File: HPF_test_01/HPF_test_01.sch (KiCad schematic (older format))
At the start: 7 parts, among them T1 GT07-110-013

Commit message: Reorganized and added footprints and symbols, .sch reflects changes
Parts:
- removed C2: 510nF, symbol pspice:C
- removed SL1002A600SP: GDT, symbol GT07:GDT
- removed SMCJ5.0A: TVS, symbol Device:D_TVS
- removed VP4032K122R300: MOV, symbol GT07:MOV
- added C2: ECQ-UBAF474K, ECQUBAF474K, symbol ECQ-UBAF474K:ECQ-UBAF474K
- added D1: SMCJ5.0A, DIONM7959X262N, symbol SMCJ5.0A:SMCJ5.0A
- added J1: BNC5-J-P-GN-RA-BH2D, BNC5-J-P-GN-RA-BH2D_kicad:BNC5JPGNRABH2D, symbol BNC5-J-P-GN-RA-BH2D:BNC5-J-P-GN-RA-BH2D
- added RV1: VP4032K122R300, CAPPM10080X500N, symbol VP4032K122R300:VP4032K122R300
- added U1: SL1002A600SP, SL1002A600SP, symbol SL1002A600SP:SL1002A600SP
- C1: footprint (none) -> Capacitor_SMD:C_0603_1608Metric_Pad1.05x0.95mm_HandSolder
- T1: footprint GT07110013 -> Kicad-GT07-models:GT07110013
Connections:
- net labels removed: out
- wire segments 22 -> 30
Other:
- moved on the sheet: C1
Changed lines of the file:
@@
 L pspice:C C1
 U 1 1 619514BE
-P 7500 4300
-F 0 "C1" H 7322 4254 50  0000 R CNN
-F 1 "220pF" H 7322 4345 50  0000 R CNN
-F 2 "" H 7500 4300 50  0001 C CNN
-F 3 "~" H 7500 4300 50  0001 C CNN
-F 4 "C" H 7500 4300 50  0001 C CNN "Spice_Primitive"
-F 5 "220p" H 7500 4300 50  0001 C CNN "Spice_Model"
-F 6 "Y" H 7500 4300 50  0001 C CNN "Spice_Netlist_Enabled"
-	1    7500 4300
+P 7450 4300
+F 0 "C1" H 7272 4254 50  0000 R CNN
+F 1 "220pF" H 7272 4345 50  0000 R CNN
+F 2 "Capacitor_SMD:C_0603_1608Metric_Pad1.05x0.95mm_HandSolder" H 7450 4300 50  0001 C CNN
+F 3 "~" H 7450 4300 50  0001 C CNN
+F 4 "C" H 7450 4300 50  0001 C CNN "Spice_Primitive"
+F 5 "220p" H 7450 4300 50  0001 C CNN "Spice_Model"
+F 6 "Y" H 7450 4300 50  0001 C CNN "Spice_Netlist_Enabled"
+	1    7450 4300
 	-1   0    0    1
-$EndComp
-Text GLabel 7600 3850 2    50   Input ~ 0
-out
-$Comp
-L pspice:0 #GND02
-U 1 1 61961008
-P 7500 4850
-F 0 "#GND02" H 7500 4750 50  0001 C CNN
-F 1 "0" H 7500 4900 50  0000 C CNN
-F 2 "" H 7500 4850 50  0001 C CNN
-F 3 "~" H 7500 4850 50  0001 C CNN
-	1    7500 4850
-	1    0    0    -1
 $EndComp
 $Comp
@@
 F 0 "T1" H 5650 4465 50  0000 C CNN
 F 1 "GT07-110-013" H 5650 4374 50  0000 C CNN
-F 2 "GT07110013" H 6200 4300 50  0001 L CNN
+F 2 "Kicad-GT07-models:GT07110013" H 6200 4300 50  0001 L CNN
 F 3 "https://componentsearchengine.com/Datasheets/1/GT07-110-013.pdf" H 6200 4200 50  0001 L CNN
 F 4 "Pulse Transformers" H 6200 4100 50  0001 L CNN "Description"
@@
 NoConn ~ 6350 4300
 NoConn ~ 4950 4300
-$Comp
-L Device:D_TVS SMCJ5.0A
-U 1 1 61BE143F
-P 6700 4300
-F 0 "SMCJ5.0A" V 6654 4380 50  0000 L CNN
-F 1 "TVS" V 6745 4380 50  0000 L CNN
-F 2 "" H 6700 4300 50  0001 C CNN
-F 3 "https://www.littelfuse.com/~/media/electronics/datasheets/tvs_diodes/littelfuse_tvs_diode_smcj_datasheet.pdf.pdf" H 6700 4300 50  0001 C CNN
-	1    6700 4300
-	0    1    1    0
-$EndComp
-$Comp
-L GT07:GDT SL1002A600SP
-U 1 1 61BE33A2
-P 4050 4000
-F 0 "SL1002A600SP" H 4278 4046 50  0000 L CNN
-F 1 "GDT" H 4278 3955 50  0000 L CNN
-F 2 "" H 4050 4000 50  0001 C CNN
-F 3 "https://www.mouser.com/datasheet/2/240/Littelfuse_GDT_SL1002A_Datasheet.pdf-1317360.pdf" H 4050 4000 50  0001 C CNN
-	1    4050 4000
-	1    0    0    -1
-$EndComp
-$Comp
-L pspice:C C2
-U 1 1 6194BCFB
-P 4550 5100
-F 0 "C2" V 4300 5100 50  0000 C CNN
-F 1 "510nF" V 4200 5100 50  0000 C CNN
-F 2 "" H 4550 5100 50  0001 C CNN
-F 3 "~" H 4550 5100 50  0001 C CNN
-F 4 "C" H 4550 5100 50  0001 C CNN "Spice_Primitive"
-F 5 "510n" H 4550 5100 50  0001 C CNN "Spice_Model"
-F 6 "Y" H 4550 5100 50  0001 C CNN "Spice_Netlist_Enabled"
-	1    4550 5100
-	0    -1   -1   0
-$EndComp
-Wire Wire Line
-	4050 3600 4950 3600
 Wire Wire Line
 	4950 3600 4950 4200
-$Comp
-L GT07:MOV VP4032K122R300
-U 1 1 61BE8782
-P 4050 4750
-F 0 "VP4032K122R300" H 4178 4796 50  0000 L CNN
-F 1 "MOV" H 4178 4705 50  0000 L CNN
-F 2 "" H 4100 4800 50  0001 C CNN
-F 3 "https://content.kemet.com/datasheets/KEM_V0005_VP.pdf" H 4100 4800 50  0001 C CNN
-	1    4050 4750
-	1    0    0    -1
-$EndComp
 Wire Wire Line
 	4950 5100 4800 5100
@@
 	4950 4400 4950 5100
 Wire Wire Line
-	4300 5100 4050 5100
-Wire Wire Line
-	4050 5100 3000 5100
-Wire Wire Line
 	3000 5100 3000 5250
-Connection ~ 4050 5100
 Wire Wire Line
 	3000 4550 3000 5100
@@
 Wire Wire Line
 	3000 3950 3000 3600
-Wire Wire Line
-	3000 3600 4050 3600
-Connection ~ 4050 3600
-Wire Wire Line
-	6350 4400 6350 4700
-Wire Wire Line
-	6350 4700 6700 4700
-Wire Wire Line
-	6350 4200 6350 3850
-Wire Wire Line
-	6350 3850 6700 3850
-Wire Wire Line
-	6700 4150 6700 3850
-Connection ~ 6700 3850
-Wire Wire Line
-	6700 4450 6700 4700
-Connection ~ 6700 4700
-Wire Wire Line
-	6700 3850 7500 3850
-Wire Wire Line
-	7500 3850 7500 4050
-Connection ~ 7500 3850
-Wire Wire Line
-	7500 3850 7600 3850
-Wire Wire Line
-	7500 4550 7500 4700
-Wire Wire Line
-	7500 4700 7500 4850
-Connection ~ 7500 4700
-Wire Wire Line
-	6700 4700 7500 4700
 Text Notes 6700 5150 0    50   ~ 0
 TVS: \n5V standoff\n6.4-7V breakdown \n9.2V max clamping
@@
 Text Notes 3500 5650 0    50   ~ 0
 MOV:\n300V rms rating\n385VDC\n470V Varistor V (typ)\n1.2kA surge I\n30J
+$Comp
+L VP4032K122R300:VP4032K122R300 RV1
+U 1 1 61CA4EFC
+P 4050 4250
+F 0 "RV1" V 4354 4378 50  0000 L CNN
+F 1 "VP4032K122R300" V 4445 4378 50  0000 L CNN
+F 2 "CAPPM10080X500N" H 4600 4300 50  0001 L CNN
+F 3 "https://www.arrow.com/en/products/vp4032k122r300/kemet-corporation?region=nac" H 4600 4200 50  0001 L CNN
+F 4 "Varistors 385V 1200A 4032" H 4600 4100 50  0001 L CNN "Description"
+F 5 "5" H 4600 4000 50  0001 L CNN "Height"
+F 6 "80-VP4032K122R300" H 4600 3900 50  0001 L CNN "Mouser Part Number"
+F 7 "https://www.mouser.co.uk/ProductDetail/KEMET/VP4032K122R300?qs=jj7GbYRQuOYGBVagWkrU5w%3D%3D" H 4600 3800 50  0001 L CNN "Mouser Price/Stock"
+F 8 "Kemet" H 4600 3700 50  0001 L CNN "Manufacturer_Name"
+F 9 "VP4032K122R300" H 4600 3600 50  0001 L CNN "Manufacturer_Part_Number"
+	1    4050 4250
+	0    1    1    0
+$EndComp
+$Comp
+L SL1002A600SP:SL1002A600SP U1
+U 1 1 61CA5911
+P 4050 4050
+F 0 "U1" H 4342 3685 50  0000 C CNN
+F 1 "SL1002A600SP" H 4342 3776 50  0000 C CNN
+F 2 "SL1002A600SP" H 4700 4150 50  0001 L CNN
+F 3 "https://componentsearchengine.com/Datasheets/1/SL1002A600SP.pdf" H 4700 4050 50  0001 L CNN
+F 4 "Gas Discharge Tubes - GDTs / Gas Plasma Arrestors GP MINIBETA 2T A600V SMD SPECIAL" H 4700 3950 50  0001 L CNN "Description"
+F 5 "4.1" H 4700 3850 50  0001 L CNN "Height"
+F 6 "576-SL1002A600SP" H 4700 3750 50  0001 L CNN "Mouser Part Number"
+F 7 "https://www.mouser.co.uk/ProductDetail/Littelfuse/SL1002A600SP?qs=95aqoVzNh5Z3taNZSmSH3g%3D%3D" H 4700 3650 50  0001 L CNN "Mouser Price/Stock"
+F 8 "LITTELFUSE" H 4700 3550 50  0001 L CNN "Manufacturer_Name"
+F 9 "SL1002A600SP" H 4700 3450 50  0001 L CNN "Manufacturer_Part_Number"
+	1    4050 4050
+	-1   0    0    1
+$EndComp
+Wire Wire Line
+	3000 3600 4050 3600
+Wire Wire Line
+	3000 5100 4050 5100
+Wire Wire Line
+	4050 4250 4050 4050
+Wire Wire Line
+	4050 3950 4050 3600
+Connection ~ 4050 3600
+Wire Wire Line
+	4050 3600 4950 3600
+Wire Wire Line
+	4050 4950 4050 5100
+Connection ~ 4050 5100
+Wire Wire Line
+	4050 5100 4300 5100
+$Comp
+L SMCJ5.0A:SMCJ5.0A D1
+U 1 1 61CA90D0
+P 6750 4000
+F 0 "D1" V 7004 4128 50  0000 L CNN
+F 1 "SMCJ5.0A" V 7095 4128 50  0000 L CNN
+F 2 "DIONM7959X262N" H 7150 4150 50  0001 L BNN
+F 3 "https://componentsearchengine.com/Datasheets/2/SMCJ5.0A.pdf" H 7150 4050 50  0001 L BNN
+F 4 "ESD Suppressors / TVS Diodes 1.5kW 5V 5% Uni-Directional" H 7150 3950 50  0001 L BNN "Description"
+F 5 "2.62" H 7150 3850 50  0001 L BNN "Height"
+F 6 "576-SMCJ5.0A" H 7150 3750 50  0001 L BNN "Mouser Part Number"
+F 7 "https://www.mouser.co.uk/ProductDetail/Littelfuse/SMCJ50A?qs=HR2RnyOI4E4RumofpgUEcw%3D%3D" H 7150 3650 50  0001 L BNN "Mouser Price/Stock"
+F 8 "LITTELFUSE" H 7150 3550 50  0001 L BNN "Manufacturer_Name"
+F 9 "SMCJ5.0A" H 7150 3450 50  0001 L BNN "Manufacturer_Part_Number"
+	1    6750 4000
+	0    1    1    0
+$EndComp
+$Comp
+L BNC5-J-P-GN-RA-BH2D:BNC5-J-P-GN-RA-BH2D J1
+U 1 1 61CAB142
+P 8050 4200
+F 0 "J1" H 8450 4465 50  0000 C CNN
+F 1 "BNC5-J-P-GN-RA-BH2D" H 8450 4374 50  0000 C CNN
+F 2 "BNC5-J-P-GN-RA-BH2D_kicad:BNC5JPGNRABH2D" H 8700 4300 50  0001 L CNN
+F 3 "http://suddendocs.samtec.com/prints/bnc5-j-p-xx-ra-bh2d-mkt.pdf" H 8700 4200 50  0001 L CNN
+F 4 "SAMTEC - BNC5-J-P-GN-RA-BH2D - RF COAXIAL, BNC JACK, 50 OHM, PCB" H 8700 4100 50  0001 L CNN "Description"
+F 5 "10.8" H 8700 4000 50  0001 L CNN "Height"
+F 6 "200-BNC5JPGNRABH2D" H 8700 3900 50  0001 L CNN "Mouser Part Number"
+F 7 "https://www.mouser.co.uk/ProductDetail/Samtec/BNC5-J-P-GN-RA-BH2D?qs=PB6%2FjmICvI2u%2FOQtySH%252B3g%3D%3D" H 8700 3800 50  0001 L CNN "Mouser Price/Stock"
+F 8 "SAMTEC" H 8700 3700 50  0001 L CNN "Manufacturer_Name"
+F 9 "BNC5-J-P-GN-RA-BH2D" H 8700 3600 50  0001 L CNN "Manufacturer_Part_Number"
+	1    8050 4200
+	1    0    0    -1
+$EndComp
+$Comp
+L ECQ-UBAF474K:ECQ-UBAF474K C2
+U 1 1 61CAD9E9
+P 4300 5100
+F 0 "C2" H 4550 5365 50  0000 C CNN
+F 1 "ECQ-UBAF474K" H 4550 5274 50  0000 C CNN
+F 2 "ECQUBAF474K" H 4650 5150 50  0001 L CNN
+F 3 "https://datasheet.datasheetarchive.com/originals/distributors/Datasheets_SAMA/6170a3d833bc371d0e684a1e7d5b0a3a.pdf" H 4650 5050 50  0001 L CNN
+F 4 "Film Capacitors 300VAC 0.47uF 10% LS=22.5mm ST" H 4650 4950 50  0001 L CNN "Description"
+F 5 "21.5" H 4650 4850 50  0001 L CNN "Height"
+F 6 "667-ECQ-UBAF474K" H 4650 4750 50  0001 L CNN "Mouser Part Number"
+F 7 "https://www.mouser.co.uk/ProductDetail/Panasonic/ECQ-UBAF474K?qs=DPoM0jnrROXQ4Aoi4rWlKg%3D%3D" H 4650 4650 50  0001 L CNN "Mouser Price/Stock"
+F 8 "Panasonic" H 4650 4550 50  0001 L CNN "Manufacturer_Name"
+F 9 "ECQ-UBAF474K" H 4650 4450 50  0001 L CNN "Manufacturer_Part_Number"
+	1    4300 5100
+	1    0    0    -1
+$EndComp
+Wire Wire Line
+	6350 4200 6350 4000
+Wire Wire Line
+	6350 4000 6750 4000
+Wire Wire Line
+	6750 4000 7450 4000
+Wire Wire Line
+	7850 4000 7850 4200
+Wire Wire Line
+	7850 4200 8050 4200
+Connection ~ 6750 4000
+Wire Wire Line
+	7450 4050 7450 4000
+Connection ~ 7450 4000
+Wire Wire Line
+	7450 4000 7850 4000
+Wire Wire Line
+	6350 4400 6350 4600
+Wire Wire Line
+	6350 4600 6750 4600
+Wire Wire Line
+	6750 4600 7450 4600
+Wire Wire Line
+	8050 4600 8050 4400
+Connection ~ 6750 4600
+Connection ~ 8050 4400
+Wire Wire Line
+	8050 4400 8050 4300
+Wire Wire Line
+	7450 4550 7450 4600
+Connection ~ 7450 4600
+Wire Wire Line
+	7450 4600 8050 4600
+Wire Wire Line
+	8850 4300 8850 4600
+Wire Wire Line
+	8850 4600 8050 4600
+Connection ~ 8050 4600
+Wire Wire Line
+	8850 4200 8850 4300
+Connection ~ 8850 4300
 $EndSCHEMATC

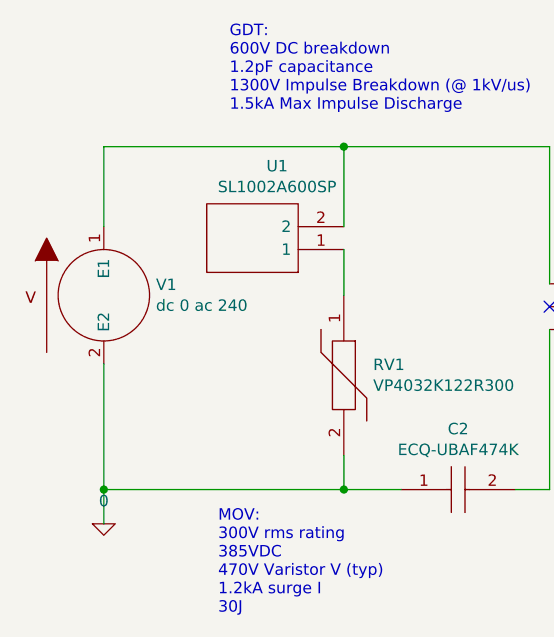
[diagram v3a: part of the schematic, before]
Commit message: added pcbnew schematic and rudimentary layout
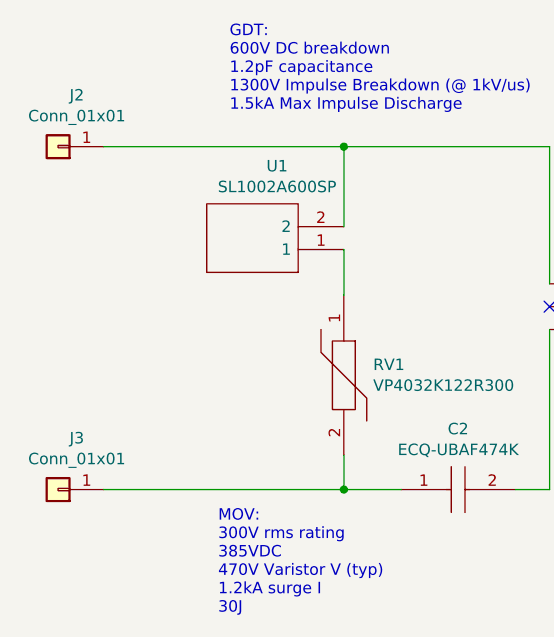
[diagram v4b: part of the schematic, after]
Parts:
- removed V1: dc 0 ac 240, symbol pspice:VSOURCE
- added J2, J3: Conn_01x01, Connector_Coaxial:SMA_Amphenol_132203-12_Horizontal, symbol Connector_Generic:Conn_01x01
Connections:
- net at T1.4 (GATE_1), U1.2: now also J2.1 (Pin_1)
- net 0: no longer names the net of C2.1, RV1.2
- net 0: now also J3.1 (Pin_1)
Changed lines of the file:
@@
 Comment4 ""
 $EndDescr
-$Comp
-L pspice:0 #GND01
-U 1 1 61933695
-P 3000 5250
-F 0 "#GND01" H 3000 5150 50  0001 C CNN
-F 1 "0" H 3000 5350 50  0000 C CNN
-F 2 "" H 3000 5250 50  0001 C CNN
-F 3 "~" H 3000 5250 50  0001 C CNN
-	1    3000 5250
-	1    0    0    -1
-$EndComp
 Text Notes 6150 4750 2    50   ~ 0
 .ac dec 10 10 1000000
@@
 	1    0    0    -1
 $EndComp
-$Comp
-L pspice:VSOURCE V1
-U 1 1 619461B3
-P 3000 4250
-F 0 "V1" H 3228 4296 50  0000 L CNN
-F 1 "dc 0 ac 240" H 3228 4205 50  0000 L CNN
-F 2 "" H 3000 4250 50  0001 C CNN
-F 3 "~" H 3000 4250 50  0001 C CNN
-F 4 "V" H 3000 4250 50  0001 C CNN "Spice_Primitive"
-F 5 "dc 0 ac 240" H 3000 4250 50  0001 C CNN "Spice_Model"
-F 6 "Y" H 3000 4250 50  0001 C CNN "Spice_Netlist_Enabled"
-	1    3000 4250
-	1    0    0    -1
-$EndComp
 NoConn ~ 6350 4300
 NoConn ~ 4950 4300
@@
 Wire Wire Line
 	4950 4400 4950 5100
-Wire Wire Line
-	3000 5100 3000 5250
-Wire Wire Line
-	3000 4550 3000 5100
-Connection ~ 3000 5100
-Wire Wire Line
-	3000 3950 3000 3600
 Text Notes 6700 5150 0    50   ~ 0
 TVS: \n5V standoff\n6.4-7V breakdown \n9.2V max clamping
@@
 	8850 4200 8850 4300
 Connection ~ 8850 4300
+$Comp
+L Connector_Generic:Conn_01x01 J2
+U 1 1 61CBC9A8
+P 2800 3600
+F 0 "J2" H 2718 3375 50  0000 C CNN
+F 1 "Conn_01x01" H 2718 3466 50  0000 C CNN
+F 2 "Connector_Coaxial:SMA_Amphenol_132203-12_Horizontal" H 2800 3600 50  0001 C CNN
+F 3 "~" H 2800 3600 50  0001 C CNN
+	1    2800 3600
+	-1   0    0    1
+$EndComp
+$Comp
+L Connector_Generic:Conn_01x01 J3
+U 1 1 61CBCE04
+P 2800 5100
+F 0 "J3" H 2718 4875 50  0000 C CNN
+F 1 "Conn_01x01" H 2718 4966 50  0000 C CNN
+F 2 "Connector_Coaxial:SMA_Amphenol_132203-12_Horizontal" H 2800 5100 50  0001 C CNN
+F 3 "~" H 2800 5100 50  0001 C CNN
+	1    2800 5100
+	-1   0    0    1
+$EndComp
 $EndSCHEMATC
